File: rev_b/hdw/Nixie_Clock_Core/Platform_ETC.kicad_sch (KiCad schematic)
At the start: 7 parts, among them U2301 DS1683

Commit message: lots of rev B control board schematic progress
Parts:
- renumbered C2304 to C?, D2301 to D?, DOC2301 to DOC?, U2301 to U?

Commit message: more rev b sch progress
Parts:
- removed C? (x2): 10uF, Capacitors_SMD:C_0603, symbol Custom_Library:C_Custom
- added C? (x2): 10uF, Capacitors_SMD:C_0603, symbol Custom_Library:C_Custom
- C? (x2), D?: Configuration (none) -> ETC
- U?: Config TOF -> ETC
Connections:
- net GND: now also C?.2, C?.2
- net at C?.1, C?.1, D?.1 (K)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: now also C?.1, C?.1
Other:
- moved on the sheet: C?

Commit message: updated footprints, ran some DRC
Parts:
- C? (x3): Digi-Key PN 490-14372-1-ND -> (none)
- C?: Digi-Key PN 311-1344-1-ND -> (none)
- D?: Digi-Key PN (none) -> 497-5711-1-ND
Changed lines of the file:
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@@
       (effects (font (size 1.27 1.27)) (justify right))
+    )
+    (property "Digi-Key PN" "497-5711-1-ND" (at 78.74 67.31 0)
+      (effects (font (size 1.27 1.27)) hide)
     )
     (pin "1")
@@
       (project "Nixie_Clock_Core"
         (path "/16fdce21-b570-4d81-a458-e8839d611806/61f04371-5be4-452b-bab3-2ded046cc354"
-          (reference "D?") (unit 1)
+          (reference "D1401") (unit 1)
         )
       )
@@
       (project "Nixie_Clock_Core"
         (path "/16fdce21-b570-4d81-a458-e8839d611806/61f04371-5be4-452b-bab3-2ded046cc354"
-          (reference "#PWR?") (unit 1)
+          (reference "#PWR01403") (unit 1)
         )
       )
@@
       (effects (font (size 1.27 1.27)) hide)
     )
-    (property "Digi-Key PN" "490-14372-1-ND" (at 122.555 67.31 0)
+    (property "Digi-Key PN" "" (at 122.555 67.31 0)
       (effects (font (size 1.524 1.524)) hide)
     )
@@
       (project "Nixie_Clock_Core"
         (path "/16fdce21-b570-4d81-a458-e8839d611806/61f04371-5be4-452b-bab3-2ded046cc354"
-          (reference "C?") (unit 1)
+          (reference "C1403") (unit 1)
         )
       )
@@
       (project "Nixie_Clock_Core"
         (path "/16fdce21-b570-4d81-a458-e8839d611806/61f04371-5be4-452b-bab3-2ded046cc354"
-          (reference "#PWR?") (unit 1)
+          (reference "#PWR01404") (unit 1)
         )
       )
@@
       (project "Nixie_Clock_Core"
         (path "/16fdce21-b570-4d81-a458-e8839d611806/61f04371-5be4-452b-bab3-2ded046cc354"
-          (reference "#FLG?") (unit 1)
+          (reference "#FLG01401") (unit 1)
         )
       )
@@
       (effects (font (size 1.27 1.27)) hide)
     )
-    (property "Digi-Key PN" "490-14372-1-ND" (at 106.045 67.31 0)
+    (property "Digi-Key PN" "" (at 106.045 67.31 0)
       (effects (font (size 1.524 1.524)) hide)
     )
@@
       (project "Nixie_Clock_Core"
         (path "/16fdce21-b570-4d81-a458-e8839d611806/61f04371-5be4-452b-bab3-2ded046cc354"
-          (reference "C?") (unit 1)
+          (reference "C1402") (unit 1)
         )
       )
@@
       (project "Nixie_Clock_Core"
         (path "/16fdce21-b570-4d81-a458-e8839d611806/61f04371-5be4-452b-bab3-2ded046cc354"
-          (reference "DOC?") (unit 1)
+          (reference "DOC1401") (unit 1)
         )
       )
@@
       (project "Nixie_Clock_Core"
         (path "/16fdce21-b570-4d81-a458-e8839d611806/61f04371-5be4-452b-bab3-2ded046cc354"
-          (reference "#PWR?") (unit 1)
+          (reference "#PWR01402") (unit 1)
         )
       )
@@
       (project "Nixie_Clock_Core"
         (path "/16fdce21-b570-4d81-a458-e8839d611806/61f04371-5be4-452b-bab3-2ded046cc354"
-          (reference "#PWR?") (unit 1)
+          (reference "#PWR01407") (unit 1)
         )
       )
@@
       (project "Nixie_Clock_Core"
         (path "/16fdce21-b570-4d81-a458-e8839d611806/61f04371-5be4-452b-bab3-2ded046cc354"
-          (reference "#PWR?") (unit 1)
+          (reference "#PWR01405") (unit 1)
         )
       )
@@
       (project "Nixie_Clock_Core"
         (path "/16fdce21-b570-4d81-a458-e8839d611806/61f04371-5be4-452b-bab3-2ded046cc354"
-          (reference "#PWR?") (unit 1)
+          (reference "#PWR01401") (unit 1)
         )
       )
@@
       (project "Nixie_Clock_Core"
         (path "/16fdce21-b570-4d81-a458-e8839d611806/61f04371-5be4-452b-bab3-2ded046cc354"
-          (reference "#PWR?") (unit 1)
+          (reference "#PWR01406") (unit 1)
         )
       )
@@
       (effects (font (size 1.27 1.27)) (justify right))
     )
-    (property "Digi-Key PN" "311-1344-1-ND" (at 128.27 80.01 0)
+    (property "Digi-Key PN" "" (at 128.27 80.01 0)
       (effects (font (size 1.27 1.27)) hide)
     )
@@
       (project "Nixie_Clock_Core"
         (path "/16fdce21-b570-4d81-a458-e8839d611806/61f04371-5be4-452b-bab3-2ded046cc354"
-          (reference "C?") (unit 1)
+          (reference "C1404") (unit 1)
         )
       )
@@
       (project "Nixie_Clock_Core"
         (path "/16fdce21-b570-4d81-a458-e8839d611806/61f04371-5be4-452b-bab3-2ded046cc354"
-          (reference "U?") (unit 1)
+          (reference "U1401") (unit 1)
         )
       )
@@
       (effects (font (size 1.27 1.27)) hide)
     )
-    (property "Digi-Key PN" "490-14372-1-ND" (at 89.535 67.31 0)
+    (property "Digi-Key PN" "" (at 89.535 67.31 0)
       (effects (font (size 1.524 1.524)) hide)
     )
@@
       (project "Nixie_Clock_Core"
         (path "/16fdce21-b570-4d81-a458-e8839d611806/61f04371-5be4-452b-bab3-2ded046cc354"
-          (reference "C?") (unit 1)
-        )
-      )
+          (reference "C1401") (unit 1)
+        )
+      )

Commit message: hid all passive refdes on core PCB
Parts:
- C? (x3): Digi-Key PN (none) -> 1276-1871-1-ND
- C?: Digi-Key PN (none) -> 1276-1935-1-ND
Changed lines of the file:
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@@
       (effects (font (size 1.27 1.27)) hide)
     )
-    (property "Digi-Key PN" "" (at 122.555 67.31 0)
+    (property "Digi-Key PN" "1276-1871-1-ND" (at 122.555 67.31 0)
       (effects (font (size 1.524 1.524)) hide)
     )
@@
       (effects (font (size 1.27 1.27)) hide)
     )
-    (property "Digi-Key PN" "" (at 106.045 67.31 0)
+    (property "Digi-Key PN" "1276-1871-1-ND" (at 106.045 67.31 0)
       (effects (font (size 1.524 1.524)) hide)
     )
@@
       (effects (font (size 1.27 1.27)) (justify right))
     )
-    (property "Digi-Key PN" "" (at 128.27 80.01 0)
+    (property "Digi-Key PN" "1276-1935-1-ND" (at 128.27 80.01 0)
       (effects (font (size 1.27 1.27)) hide)
     )
@@
       (effects (font (size 1.27 1.27)) hide)
     )
-    (property "Digi-Key PN" "" (at 89.535 67.31 0)
-      (effects (font (size 1.524 1.524)) hide)
-    )
+    (property "Digi-Key PN" "1276-1871-1-ND" (at 89.535 67.31 0)
+      (effects (font (size 1.524 1.524)) hide)
+    )

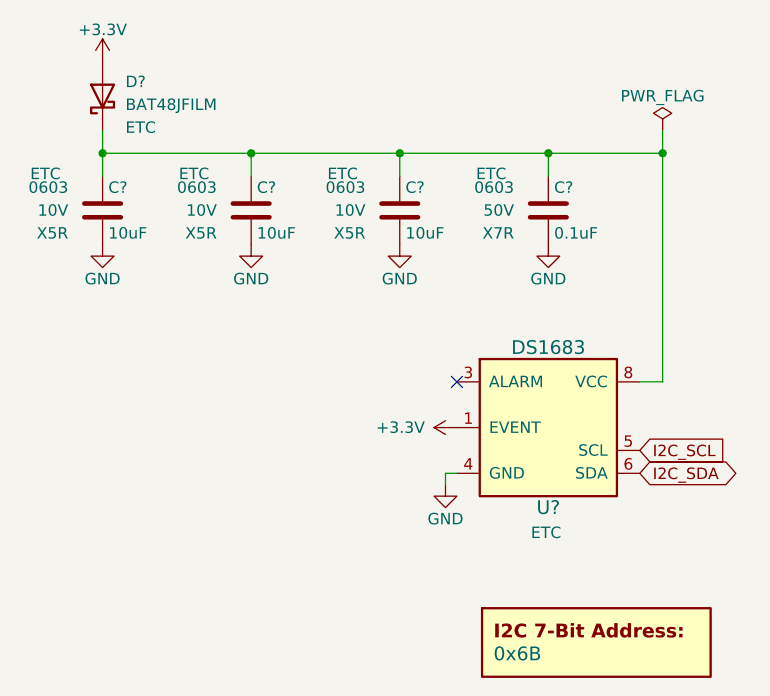
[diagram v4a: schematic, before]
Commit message: added BOM
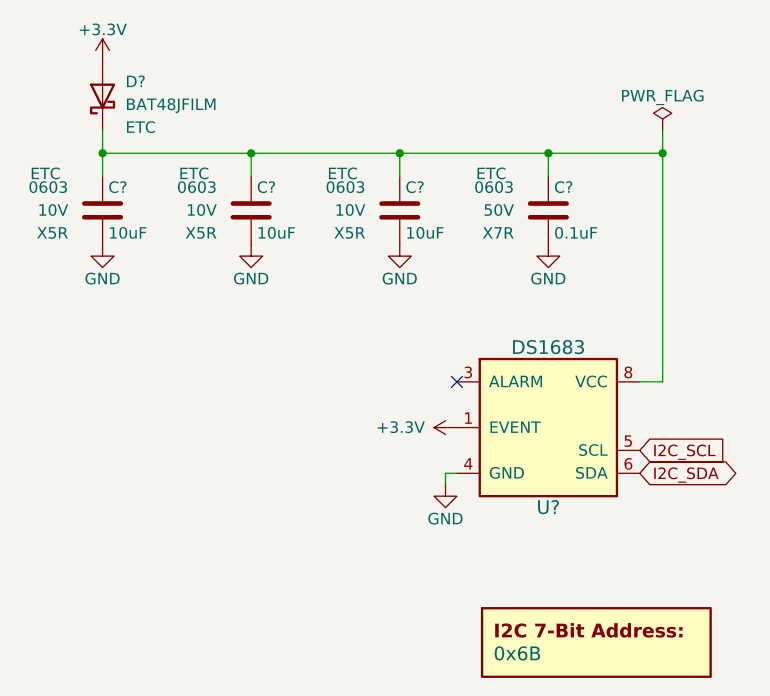
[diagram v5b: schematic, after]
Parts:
- U?: Config ETC -> (none); Configuration (none) -> ETC
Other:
- title: (none) -> Nixie Clock Redux Core Board
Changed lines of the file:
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@@
   (paper "A")
   (title_block
-    (date "2023-05-12")
-    (rev "PRELIM")
+    (title "Nixie Clock Redux Core Board")
+    (date "2023-07-30")
+    (rev "B")
     (company "Drew Maatman")
   )
@@
     (stroke (width 0) (type default))
   )
-  (global_label "I2C_SCL" (shape input) (at 138.43 106.68 0)
+  (global_label "I2C_SCL" (shape input) (at 138.43 106.68 0) (fields_autoplaced)
     (effects (font (size 1.27 1.27)) (justify left))
-    (property "Intersheetrefs" "${INTERSHEET_REFS}" (at 138.43 106.68 0)
-      (effects (font (size 1.27 1.27)) hide)
-    )
-  )
-  (global_label "I2C_SDA" (shape bidirectional) (at 138.43 109.22 0)
+    (property "Intersheetrefs" "${INTERSHEET_REFS}" (at 148.8953 106.68 0)
+      (effects (font (size 1.27 1.27)) (justify left))
+    )
+  )
+  (global_label "I2C_SDA" (shape bidirectional) (at 138.43 109.22 0) (fields_autoplaced)
     (effects (font (size 1.27 1.27)) (justify left))
-    (property "Intersheetrefs" "${INTERSHEET_REFS}" (at 138.43 109.22 0)
-      (effects (font (size 1.27 1.27)) hide)
+    (property "Intersheetrefs" "${INTERSHEET_REFS}" (at 150.0671 109.22 0)
+      (effects (font (size 1.27 1.27)) (justify left))
     )
   )
@@
       (effects (font (size 1.524 1.524)) hide)
     )
-    (property "Config" "ETC" (at 128.016 115.824 0)
-      (effects (font (size 1.27 1.27)))
-    )
-    (pin "1")
+    (property "Config" "" (at 128.016 115.824 0)
+      (effects (font (size 1.27 1.27)))
+    )
+    (property "Configuration" "ETC" (at 128.27 104.14 0)
+      (effects (font (size 1.27 1.27)) hide)
+    )
+    (pin "1")
